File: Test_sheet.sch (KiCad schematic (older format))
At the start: 1 part

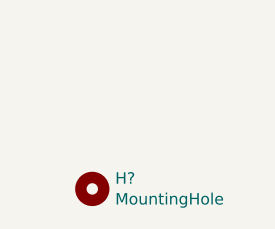
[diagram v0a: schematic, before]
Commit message: Rename subsheet
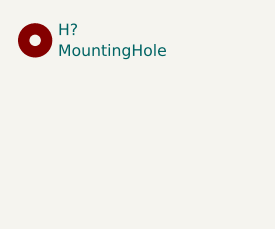
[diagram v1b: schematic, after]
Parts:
- removed H?: MountingHole, symbol Mechanical:MountingHole
- added H?: MountingHole, symbol Mechanical:MountingHole
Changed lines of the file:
@@
 $Comp
 L Mechanical:MountingHole H?
-U 1 1 614A4D60
-P 3200 3850
-F 0 "H?" H 3300 3896 50  0000 L CNN
-F 1 "MountingHole" H 3300 3805 50  0000 L CNN
-F 2 "" H 3200 3850 50  0001 C CNN
-F 3 "~" H 3200 3850 50  0001 C CNN
-	1    3200 3850
+U 1 1 614A4EF9
+P 2950 3200
+F 0 "H?" H 3050 3246 50  0000 L CNN
+F 1 "MountingHole" H 3050 3155 50  0000 L CNN
+F 2 "" H 2950 3200 50  0001 C CNN
+F 3 "~" H 2950 3200 50  0001 C CNN
+	1    2950 3200
 	1    0    0    -1
 $EndComp
